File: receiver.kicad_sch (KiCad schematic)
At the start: 2 parts, among them U1 AD8334ACPZ, U4 AD8334ACPZ

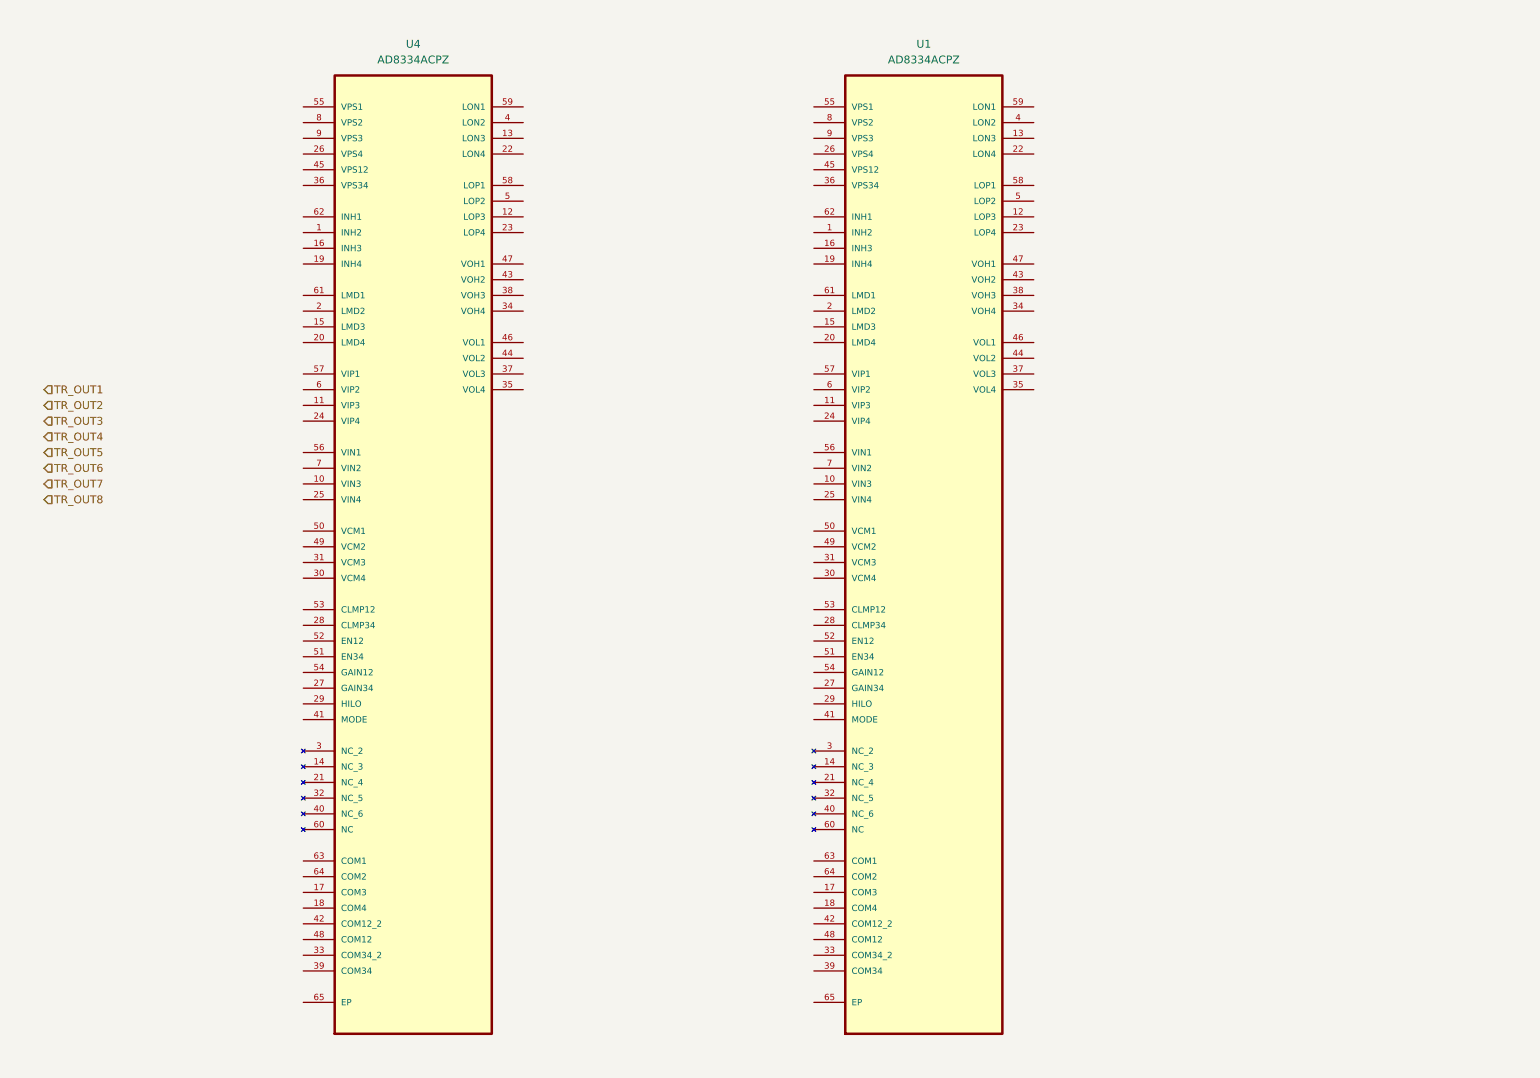
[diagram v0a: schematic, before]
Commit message: finished pulser & mcu, receiver & power remaining
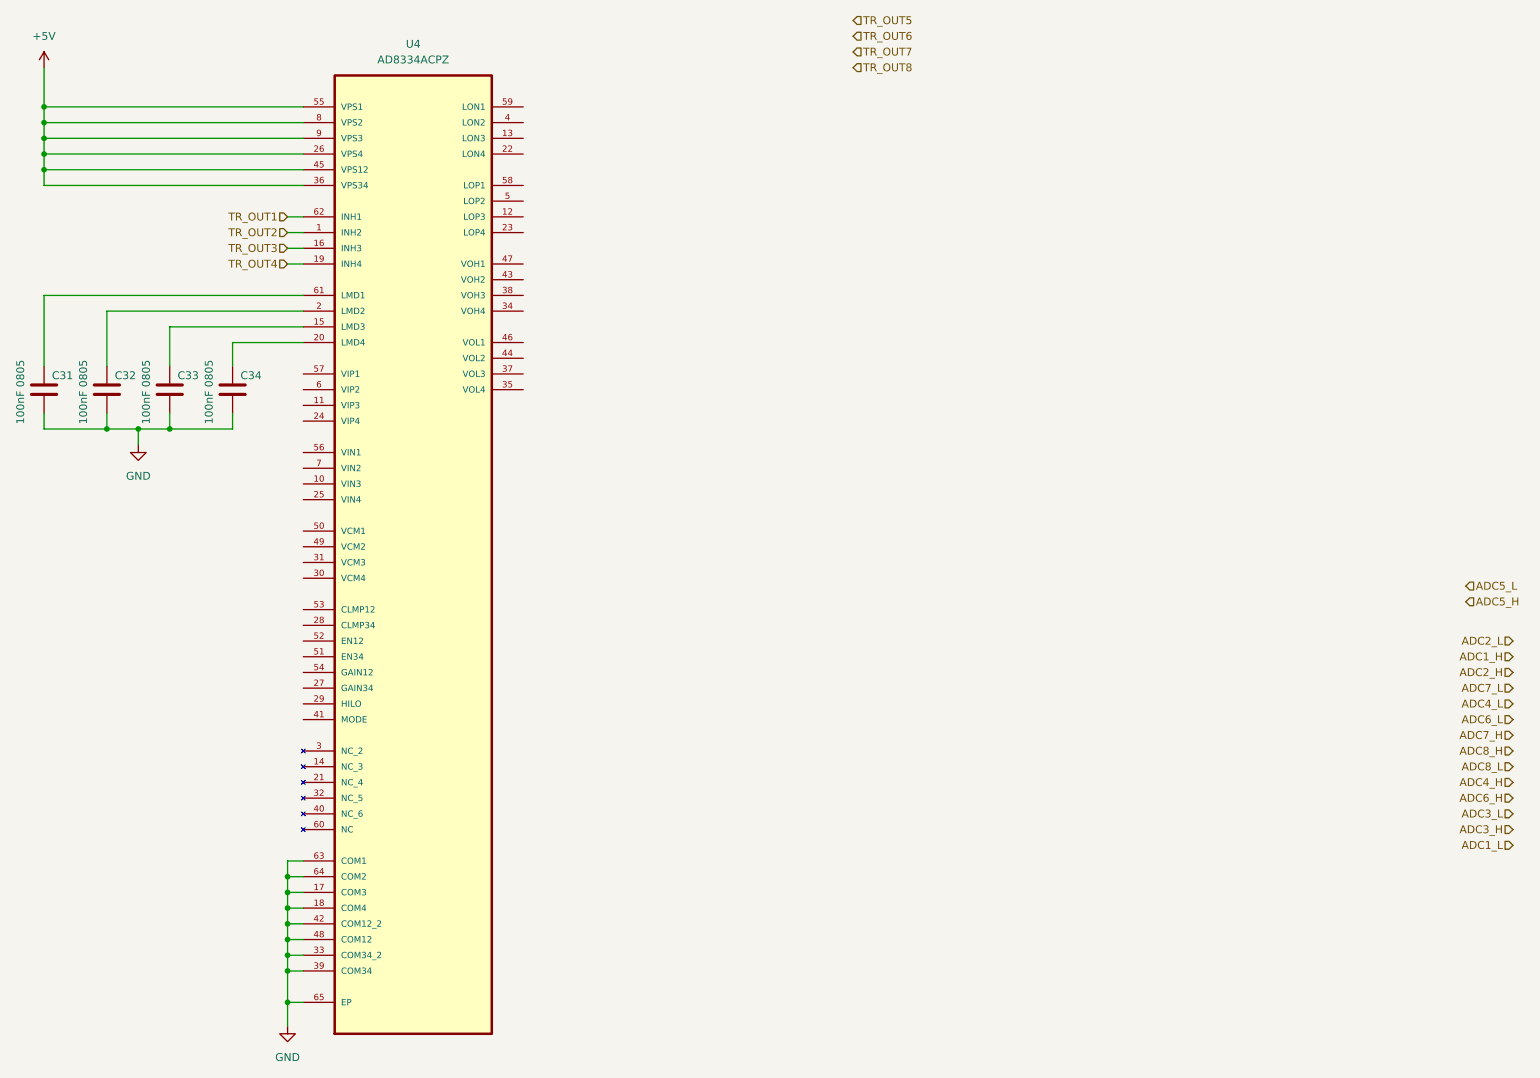
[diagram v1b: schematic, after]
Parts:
- removed U1: AD8334ACPZ, AD8334ACPZ:QFN50P900X900X100-65N, symbol AD8334ACPZ:AD8334ACPZ
- added C31, C32, C33, C34: 100nF 0805, symbol Device:C
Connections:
- net TR_OUT1: now also U4.62 (INH1)
- net TR_OUT2: now also U4.1 (INH2)
- net TR_OUT3: now also U4.16 (INH3)
- net TR_OUT4: now also U4.19 (INH4)
- net at U4.15 (LMD3): now also C33.1
- net GND: now reaches U4.17 (COM3)
- net GND: now also U4.18 (COM4), U4.33 (COM34_2), U4.39 (COM34), U4.42 (COM12_2), U4.48 (COM12), U4.63 (COM1), U4.64 (COM2), U4.65 (EP), C31.2, C32.2, C33.2, C34.2
- net at U4.2 (LMD2): now also C32.1
- net at U4.20 (LMD4): now also C34.1
- net +5V: now reaches U4.26 (VPS4)
- net +5V: now also U4.36 (VPS34), U4.45 (VPS12), U4.55 (VPS1), U4.8 (VPS2), U4.9 (VPS3)
- net at U4.61 (LMD1): now also C31.1

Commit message: converted diff signals to single-ended, modified pulser & MCU, power untouched
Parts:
- added C35, C36, C37, C38, C57, C60, C63, C66: 22pF 0805, symbol Device:C
- added C39, C40, C41, C42, C43, C44, C45, C46, C49, C51, C53, C55, C58, C59, C64, C65, C69, C72, C73, C74, C75, C76, C77, C78, C79, C80, C81, C82, C83, C84: 100nF 0805, symbol Device:C
- added C47, C48, C67, C68: 22nF 0805, symbol Device:C
- added C50, C52, C54, C56, C61, C62, C70, C71: 1nF 0805, symbol Device:C
- added JP10, JP13, JP14, JP15, JP16, JP6, JP8, JP9: SolderJumper_2_Open, symbol Jumper:SolderJumper_2_Open
- added JP11, JP12, JP4, JP5: SolderJumper_3_Open, symbol Jumper:SolderJumper_3_Open
- added L1, L2, L3, L4: 100uH 0805, symbol Device:L
- added R32, R33, R34, R35, R44, R45, R46, R47: 280R 0805, symbol Device:R
- added R36, R37, R42, R43: 500R 0805, symbol Device:R
- added R38, R40: 90R 0805, symbol Device:R
- added R39, R41: 90R 0806, symbol Device:R
- added R51, R52, R55, R56, R59, R60, R62, R63, R67, R68, R70, R71, R78, R79, R81, R82: 2.7k, symbol Device:R
- added R53, R54, R57, R58, R61, R64, R65, R66, R69, R72, R73, R74, R75, R76, R77, R80: 3.9k, symbol Device:R
- added U1: AD8334ACPZ, AD8334ACPZ:QFN50P900X900X100-65N, symbol AD8334ACPZ:AD8334ACPZ
- added U8, U9: TLV9354IDR, SOIC_9354IDR_TEX, symbol 2025-12-09_22-36-51:TLV9354IDR
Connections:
- net +5V: now also C83.1, C84.1, JP11.3 (B), JP12.3 (B), JP4.3 (B), JP5.3 (B), R36.1, R37.1, R42.1, R43.1, U1.26 (VPS4), U1.36 (VPS34), U1.45 (VPS12), U1.55 (VPS1), U1.8 (VPS2), U1.9 (VPS3), U8.4 (V+), U9.4 (V+)
- net ADC1_H: now also U4.47 (VOH1), R52.2, R60.2, U1.47 (VOH1)
- net ADC1_L: now also U4.46 (VOL1), R51.2, R59.2, U1.46 (VOL1)
- net ADC2_H: now also U4.43 (VOH2), R55.2, R62.2, U1.43 (VOH2)
- net ADC2_L: now also U4.44 (VOL2), R56.2, R63.2, U1.44 (VOL2)
- net ADC3_H: now also U4.38 (VOH3), U1.38 (VOH3)
- net ADC3_L: now also U4.37 (VOL3), U1.37 (VOL3)
- net ADC4_H: now also U4.34 (VOH4), U1.34 (VOH4)
- net ADC4_L: now also U4.35 (VOL4), U1.35 (VOL4)
- net ADC5_H: now also R68.2
- net ADC5_L: now also R67.2
- net ADC6_H: now also R70.2
- net ADC6_L: now also R71.2
- net ADC7_H: now also R78.2
- net ADC7_L: now also R79.2
- net ADC8_H: now also R82.2
- net ADC8_L: now also R81.2
- net GND: now also C35.2, C36.2, C37.2, C38.2, C47.2, C48.2, C49.2, C50.2, C51.2, C52.2, C53.2, C54.2, C55.2, C56.2, C57.2, C58.2, C59.2, C60.2, C61.2, C62.2, C63.2, C64.2, C65.2, C66.2, C67.2, C68.2, C69.2, C70.2, C71.2, C72.2, C73.2, C74.2, C83.2, C84.2, JP11.1 (A), JP12.1 (A), JP4.1 (A), JP5.1 (A), R54.1, R57.1, R61.1, R64.1, R69.1, R72.1, R77.1, R80.1, U1.17 (COM3), U1.18 (COM4), U1.33 (COM34_2), U1.39 (COM34), U1.42 (COM12_2), U1.48 (COM12), U1.63 (COM1), U1.64 (COM2), U1.65 (EP), U8.11 (V), U9.11 (V)
- net TR_OUT1: now also C35.1, R35.1
- net TR_OUT2: now also C36.1, R34.1
- net TR_OUT3: now also C37.1, R33.1
- net TR_OUT4: now also C38.1, R32.1
- net TR_OUT5: now also C57.1, R47.1, U1.62 (INH1)
- net TR_OUT6: now also C60.1, R46.1, U1.1 (INH2)
- net TR_OUT7: now also C63.1, R45.1, U1.16 (INH3)
- net TR_OUT8: now also C66.1, R44.1, U1.19 (INH4)
- net VGAA3_N: now reaches U4.10 (VIN3)
- net VGAA3_N: now also C41.2
- net VGAA3_P: now reaches U4.11 (VIP3)
- net VGAA3_P: now also C45.2
- net LNAA3_P: now reaches U4.12 (LOP3)
- net LNAA3_P: now also C45.1, C81.1, U1.12 (LOP3)
- net LNAA3_N: now reaches U4.13 (LON3)
- net LNAA3_N: now also C41.1, C77.1, R33.2, R45.2, U1.13 (LON3)
- net LNAA4_N: now reaches U4.22 (LON4)
- net LNAA4_N: now also C42.1, C78.1, R32.2, R44.2, U1.22 (LON4)
- net LNAA4_P: now reaches U4.23 (LOP4)
- net LNAA4_P: now also C46.1, C82.1, U1.23 (LOP4)
- net VGAA4_P: now reaches U4.24 (VIP4)
- net VGAA4_P: now also C46.2
- net VGAA4_N: now reaches U4.25 (VIN4)
- net VGAA4_N: now also C42.2
- net GAIN34_A: now reaches U4.27 (GAIN34)
- net GAIN34_A: now also C48.1, L2.2
- net CLAMP34_A: now reaches U4.28 (CLMP34)
- net HILO_A: now reaches U4.29 (HILO)
- net HILO_A: now also JP5.2 (C)
- net at U4.30 (VCM4): now also JP10.2 (B)
- net at U4.31 (VCM3): now also JP9.2 (B)
- net LNAA2_N: now reaches U4.4 (LON2)
- net LNAA2_N: now also C40.1, C76.1, R34.2, R46.2, U1.4 (LON2)
- net MODE_A: now reaches U4.41 (MODE)
- net MODE_A: now also JP4.2 (C)
- net at U4.49 (VCM2): now also JP8.2 (B)
- net LNAA2_P: now reaches U4.5 (LOP2)
- net LNAA2_P: now also C44.1, C80.1, U1.5 (LOP2)
- net at U4.50 (VCM1): now also JP6.2 (B)
- net EN34_A: now reaches U4.51 (EN34)
- net EN34_A: now also R36.2
- net EN12_A: now reaches U4.52 (EN12)
- net EN12_A: now also R37.2
- net CLAMP12_A: now reaches U4.53 (CLMP12)
- net GAIN12_A: now reaches U4.54 (GAIN12)
- net GAIN12_A: now also C47.1, L1.2
- net VGAA1_N: now reaches U4.56 (VIN1)
- net VGAA1_N: now also C39.2
- net VGAA1_P: now reaches U4.57 (VIP1)
- net VGAA1_P: now also C43.2
- net LNAA1_P: now reaches U4.58 (LOP1)
- net LNAA1_P: now also C43.1, C79.1, U1.58 (LOP1)
- net LNAA1_N: now reaches U4.59 (LON1)
- net LNAA1_N: now also C39.1, C75.1, R35.2, R47.2, U1.59 (LON1)
- net VGAA2_P: now reaches U4.6 (VIP2)
- net VGAA2_P: now also C44.2
- net VGAA2_N: now reaches U4.7 (VIN2)
- net VGAA2_N: now also C40.2
- new net: R80.2, R82.1, U9.12 (+IN_D)
- new net: R77.2, R78.1, U9.10 (+IN_C)
- new net: R76.1, R81.1, U9.13 (IN_D)
- new net: R67.1, R73.1, U9.2 (IN_A)
- new net: R68.1, R69.2, U9.3 (+IN_A)
- new net: R70.1, R72.2, U9.5 (+IN_B)
- new net: R71.1, R74.2, U9.6 (IN_B)
- new net: R75.2, R79.1, U9.9 (IN_C)
- new net: C72.1, U1.2 (LMD2)
- new net: R60.1, R61.2, U8.12 (+IN_D)
- new net: L1.1, R38.2
- new net: R51.1, R53.1, U8.2 (IN_A)
- new net: R52.1, R54.2, U8.3 (+IN_A)
- new net: JP16.2 (B), U1.30 (VCM4)
- new net: C73.1, U1.15 (LMD3)
- new net: R63.1, R66.2, U8.9 (IN_C)
- new net: C74.1, U1.20 (LMD4)
- new net: C69.1, U1.61 (LMD1)
- new net: JP15.2 (B), U1.31 (VCM3)
- new net: JP14.2 (B), U1.49 (VCM2)
- new net: JP13.2 (B), U1.50 (VCM1)
- new net: L3.1, R40.2
- new net: R62.1, R64.2, U8.10 (+IN_C)
- new net: L2.1, R39.2
- new net: R59.1, R65.1, U8.13 (IN_D)
- new net: L4.1, R41.2
- new net: R56.1, R58.2, U8.6 (IN_B)
- new net: R55.1, R57.2, U8.5 (+IN_B)
- new net 1.5V: C49.1, C50.1, C51.1, C52.1, C53.1, C54.1, C55.1, C56.1, C58.1, C59.1, C61.1, C62.1, C64.1, C65.1, C70.1, C71.1, JP10.1 (A), JP13.1 (A), JP14.1 (A), JP15.1 (A), JP16.1 (A), JP6.1 (A), JP8.1 (A), JP9.1 (A)
- new net ADC1: R53.2, U8.1 (OUT_A)
- new net ADC2: R58.1, U8.7 (OUT_B)
- new net ADC3: R66.1, U8.8 (OUT_C)
- new net ADC4: R65.2, U8.14 (OUT_D)
- new net ADC5: R73.2, U9.1 (OUT_A)
- new net ADC6: R74.1, U9.7 (OUT_B)
- new net ADC7: R75.1, U9.8 (OUT_C)
- new net ADC8: R76.2, U9.14 (OUT_D)
- new net AFE_GAIN_A1: R38.1
- new net AFE_GAIN_A2: R39.1
- new net AFE_GAIN_B1: R40.1
- new net AFE_GAIN_B2: R41.1
- new net CLAMP12_B: U1.53 (CLMP12)
- new net CLAMP34_B: U1.28 (CLMP34)
- new net EN12_B: R43.2, U1.52 (EN12)
- new net EN34_B: R42.2, U1.51 (EN34)
- new net GAIN12_B: C67.1, L3.2, U1.54 (GAIN12)
- new net GAIN34_B: C68.1, L4.2, U1.27 (GAIN34)
- new net HILO_B: JP12.2 (C), U1.29 (HILO)
- new net MODE_B: JP11.2 (C), U1.41 (MODE)
- new net VGAA5_N: C75.2, U1.56 (VIN1)
- new net VGAA5_P: C79.2, U1.57 (VIP1)
- new net VGAA6_N: C76.2, U1.7 (VIN2)
- new net VGAA6_P: C80.2, U1.6 (VIP2)
- new net VGAA7_N: C77.2, U1.10 (VIN3)
- new net VGAA7_P: C81.2, U1.11 (VIP3)
- new net VGAA8_N: C78.2, U1.25 (VIN4)
- new net VGAA8_P: C82.2, U1.24 (VIP4)
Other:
- note added: "0.5k would draw 10mA, acceptable."
- note added: "2nd order filter values were recommended by a TI application note (spraa88a), specs: - PWM frequency = 5 MHz - Cut-off frequency = 107.3 KHz - Damping ratio = 0.675 (over-damped but response time = 3 uSec)"
- moved on the sheet: C31, C32, C33, C34, U4

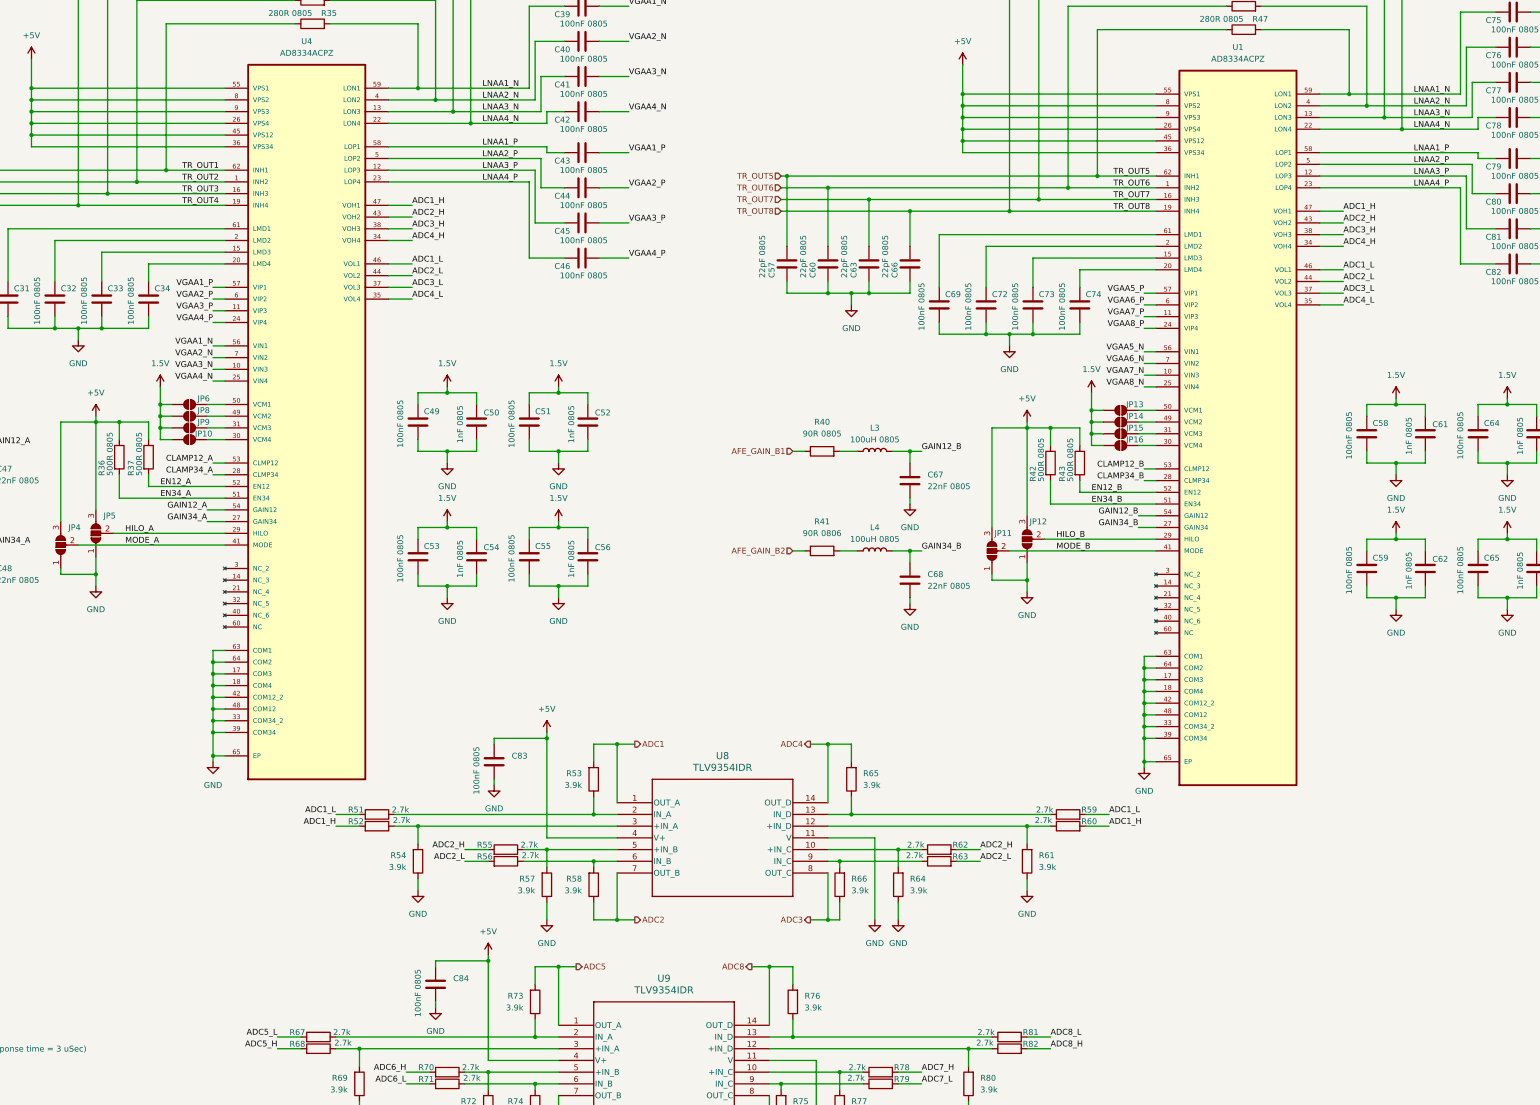
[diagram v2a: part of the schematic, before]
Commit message: finished analog signal chain, added main power components, complete the schematic and form a power budget table
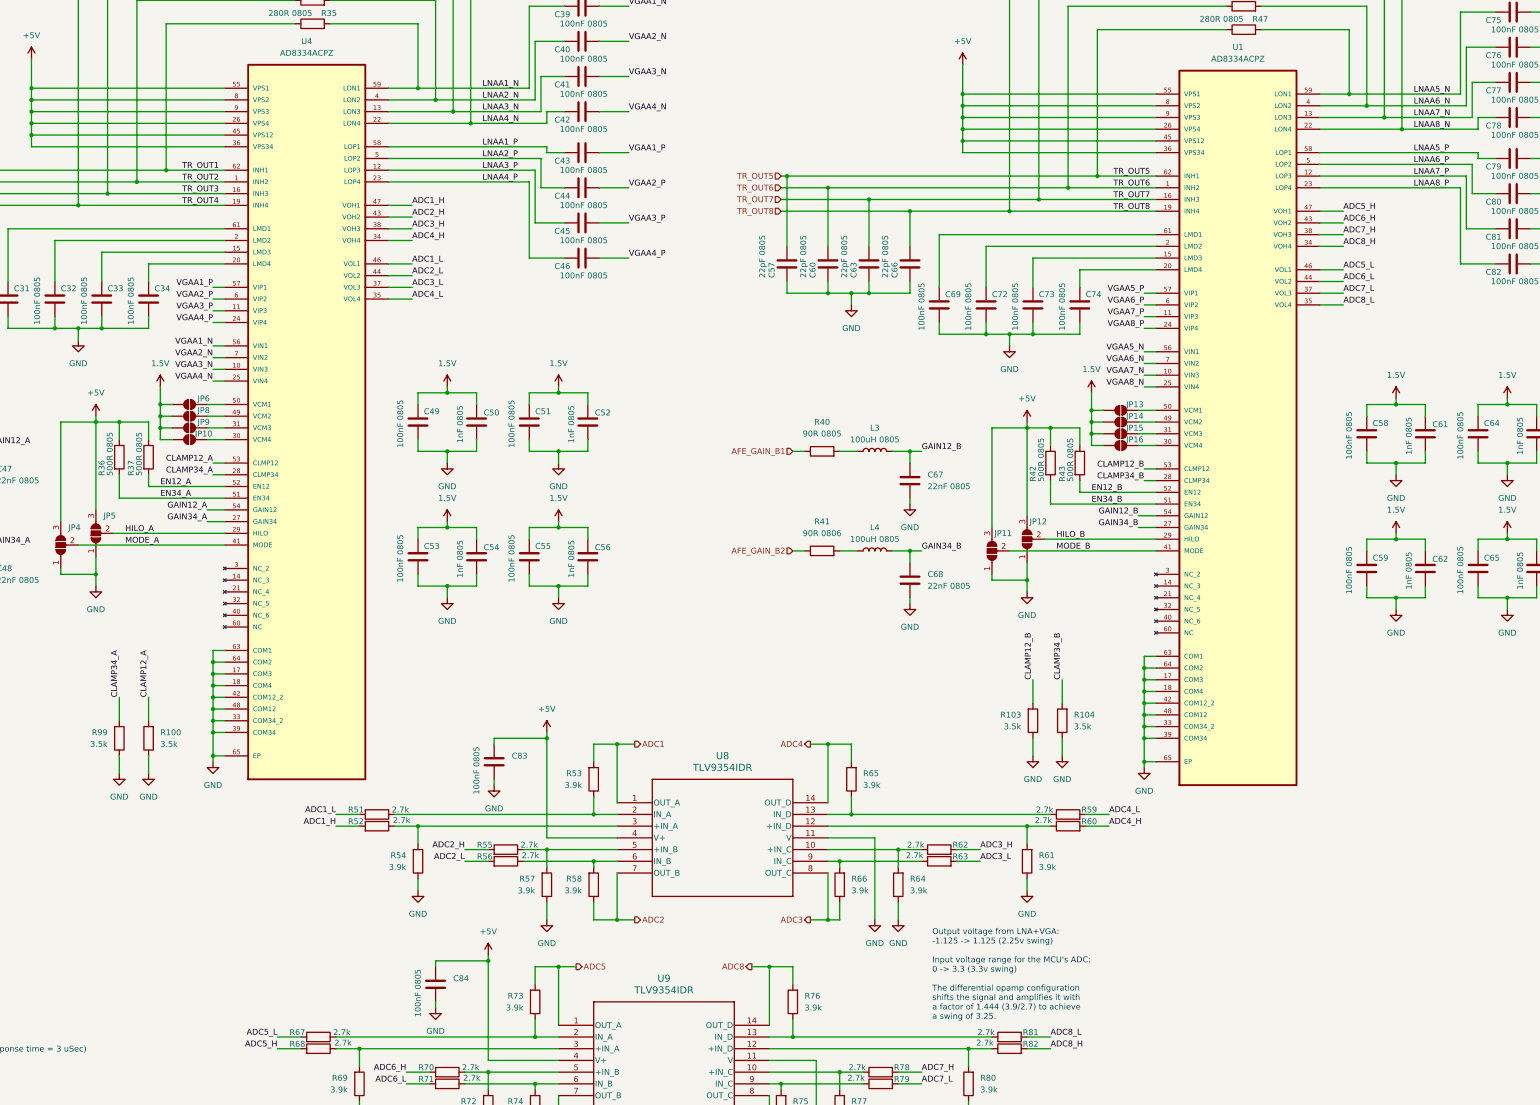
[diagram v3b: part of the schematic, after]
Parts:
- added R100, R103, R104, R99: 3.5k, symbol Device:R
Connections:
- net ADC1_H: no longer R60.2, U1.47 (VOH1)
- net ADC1_L: no longer R59.2, U1.46 (VOL1)
- net ADC2_H: no longer R62.2, U1.43 (VOH2)
- net ADC2_L: no longer R63.2, U1.44 (VOL2)
- net ADC3_H: now also R62.2; no longer U1.38 (VOH3)
- net ADC3_L: now also R63.2; no longer U1.37 (VOL3)
- net ADC4_H: now also R60.2; no longer U1.34 (VOH4)
- net ADC4_L: now also R59.2; no longer U1.35 (VOL4)
- net ADC5_H: now also U1.47 (VOH1)
- net ADC5_L: now also U1.46 (VOL1)
- net ADC6_H: now also U1.43 (VOH2)
- net ADC6_L: now also U1.44 (VOL2)
- net ADC7_H: now also U1.38 (VOH3)
- net ADC7_L: now also U1.37 (VOL3)
- net ADC8_H: now also U1.34 (VOH4)
- net ADC8_L: now also U1.35 (VOL4)
- net CLAMP12_A: now also R100.2
- net CLAMP12_B: now also R103.2
- net CLAMP34_A: now also R99.2
- net CLAMP34_B: now also R104.2
- net GND: now also R100.1, R103.1, R104.1, R99.1
- net LNAA1_N: no longer C75.1, R47.2, U1.59 (LON1)
- net LNAA1_P: no longer C79.1, U1.58 (LOP1)
- net LNAA2_N: no longer C76.1, R46.2, U1.4 (LON2)
- net LNAA2_P: no longer C80.1, U1.5 (LOP2)
- net LNAA3_N: no longer C77.1, R45.2, U1.13 (LON3)
- net LNAA3_P: no longer C81.1, U1.12 (LOP3)
- net LNAA4_N: no longer C78.1, R44.2, U1.22 (LON4)
- net LNAA4_P: no longer C82.1, U1.23 (LOP4)
- new net LNAA5_N: C75.1, R47.2, U1.59 (LON1)
- new net LNAA5_P: C79.1, U1.58 (LOP1)
- new net LNAA6_N: C76.1, R46.2, U1.4 (LON2)
- new net LNAA6_P: C80.1, U1.5 (LOP2)
- new net LNAA7_N: C77.1, R45.2, U1.13 (LON3)
- new net LNAA7_P: C81.1, U1.12 (LOP3)
- new net LNAA8_N: C78.1, R44.2, U1.22 (LON4)
- new net LNAA8_P: C82.1, U1.23 (LOP4)
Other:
- note added: "Output voltage from LNA+VGA: -1.125 -> 1.125 (2.25v swing) Input voltage range for the MCU's ADC: 0 -> 3.3 (3.3v swing) The differential opamp configuration shifts the signal and amplifies it with a factor of 1.444 (3.9/2.7) to achieve a swing of 3.25."
